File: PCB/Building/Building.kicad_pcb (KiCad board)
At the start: 2 copper layers, 95 x 60.5 mm, 37 parts, among them J1 Conn_01x05, U1 HT16K33-28SOP

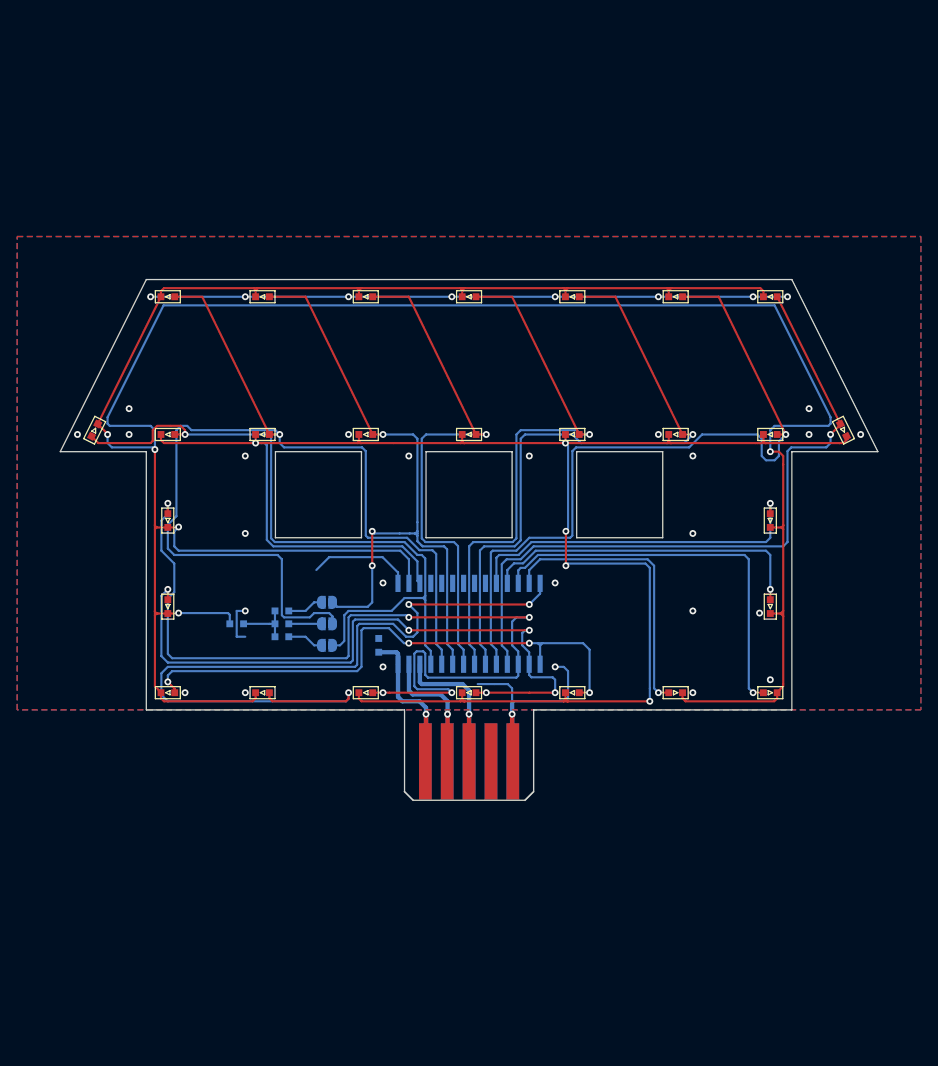
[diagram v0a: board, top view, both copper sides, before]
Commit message: (Building) 回路図内のラベルを3セット独立に修正 #75
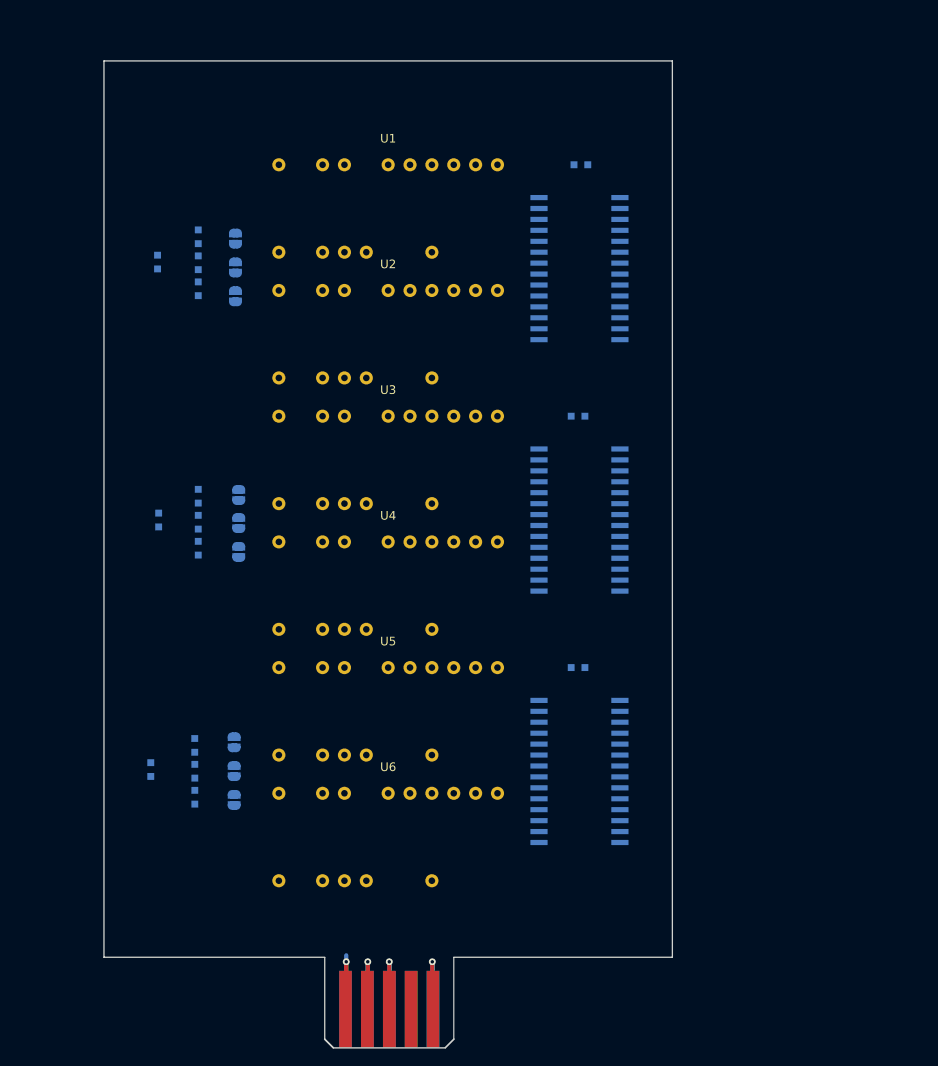
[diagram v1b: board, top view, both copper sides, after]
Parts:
- removed D10, D11, D12, D13, D14, D15, D16, D17, D18, D19, D20, D21, D22, D23, D24, D25, D26, D27, D4, D5, D6, D7, D8, D9: LED, extsui:LED_1608_HandSolderingCustom
- removed D28: D, extsui:LED_1608_HandSolderingCustom
- added C2: 0.1u, extsui:C_1608_HandSolderingCustom, B.Cu at (160.2, 65.9)
- added C3: 0.1u, extsui:C_1608_HandSolderingCustom, B.Cu at (160.2, 95.1)
- added IC1: HT16K33-28SOP, Package_SO:SOIC-28W_7.5x18.7mm_P1.27mm, B.Cu at (160.3, 48.7)
- added IC2: HT16K33-28SOP, Package_SO:SOIC-28W_7.5x18.7mm_P1.27mm, B.Cu at (160.3, 77.9)
- added IC3: HT16K33-28SOP, Package_SO:SOIC-28W_7.5x18.7mm_P1.27mm, B.Cu at (160.3, 107.2)
- added JP4: A0, Jumper:SolderJumper-2_P1.3mm_Open_RoundedPad1.0x1.5mm, B.Cu at (120.2, 110.5)
- added JP5: A1, Jumper:SolderJumper-2_P1.3mm_Open_RoundedPad1.0x1.5mm, B.Cu at (120.2, 107.1)
- added JP6: A2, Jumper:SolderJumper-2_P1.3mm_Open_RoundedPad1.0x1.5mm, B.Cu at (120.2, 103.8)
- added JP7: A0, Jumper:SolderJumper-2_P1.3mm_Open_RoundedPad1.0x1.5mm, B.Cu at (120.7, 75.0)
- added JP8: A1, Jumper:SolderJumper-2_P1.3mm_Open_RoundedPad1.0x1.5mm, B.Cu at (120.7, 78.3)
- added JP9: A2, Jumper:SolderJumper-2_P1.3mm_Open_RoundedPad1.0x1.5mm, B.Cu at (120.7, 81.6)
- added R4: 39k, extsui:R_1608_HandSolderingCustom, B.Cu at (116.0, 75.2)
- added R5: 39k, extsui:R_1608_HandSolderingCustom, B.Cu at (116.0, 78.2)
- added R6: 39k, extsui:R_1608_HandSolderingCustom, B.Cu at (116.0, 81.2)
- added R7: 39k, extsui:R_1608_HandSolderingCustom, B.Cu at (115.6, 107.1)
- added R8: 39k, extsui:R_1608_HandSolderingCustom, B.Cu at (115.6, 104.1)
- added R9: 39k, extsui:R_1608_HandSolderingCustom, B.Cu at (115.6, 110.1)
- added U2: OSL60362_IX, extsui:OSL60362_XX, F.Cu at (138.1, 56.4)
- added U3: OSL60362_IX, extsui:OSL60362_XX, F.Cu at (138.1, 71.0)
- added U4: OSL60362_IX, extsui:OSL60362_XX, F.Cu at (138.1, 85.6)
- added U5: OSL60362_IX, extsui:OSL60362_XX, F.Cu at (138.1, 100.2)
- added U6: OSL60362_IX, extsui:OSL60362_XX, F.Cu at (138.1, 114.8)
- D1, D2, D3: value LED -> D; moved to B.Cu
- JP1: value A2 -> A0
- JP3: value A0 -> A2
- U1: value HT16K33-28SOP -> OSL60362_IX; footprint Package_SO:SOIC-28W_7.5x18.7mm_P1.27mm -> extsui:OSL60362_XX; moved to F.Cu
- moved C1 60.6 mm to (160.5, 36.7), turned to 0 degrees
- moved D3 56.4 mm to (110.5, 106.9), turned to 90 degrees
- moved U1 49.2 mm to (138.1, 41.7), turned to 0 degrees
- moved JP1 48.4 mm to (120.4, 45.2), turned to 90 degrees
- moved R1 47.5 mm to (116.0, 45.0), turned to 90 degrees
- moved R2 43.1 mm to (116.0, 48.1), turned to 90 degrees
- moved JP2 42.8 mm to (120.4, 48.6), turned to 90 degrees
- moved R3 38.7 mm to (116.0, 51.1), turned to 90 degrees
- moved JP3 37.1 mm to (120.4, 51.9), turned to 90 degrees
- moved J1 30.2 mm to (138.2, 134.8)
- moved D2 26.0 mm to (111.4, 77.9), turned to 90 degrees
- moved D1 20.9 mm to (111.3, 48.0), turned to 90 degrees
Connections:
- D1 pad 2: Net-(D1-Pad2) -> /A_1
- D2 pad 1: Net-(D1-Pad1) -> Net-(D2-Pad1)
- D2 pad 2: Net-(D18-Pad2) -> /A_2
- D3 pad 1: Net-(D1-Pad1) -> Net-(D3-Pad1)
- D3 pad 2: Net-(D19-Pad2) -> /A_3
- JP1 pad 2: Net-(D1-Pad2) -> /CA3
- JP2 pad 2: Net-(D18-Pad2) -> /CA2
- JP3 pad 2: Net-(D19-Pad2) -> /CA1
- R1 pad 2: Net-(D28-Pad1) -> Net-(D1-Pad1)
- R2 pad 2: Net-(D28-Pad1) -> Net-(D1-Pad1)
- R3 pad 2: Net-(D28-Pad1) -> Net-(D1-Pad1)
- U1 pad 1: GND -> /E_1
- U1 pad 12: Net-(D14-Pad2) -> /CA6
- U1 pad 13: Net-(D13-Pad2) -> /CA5
- U1 pad 14: Net-(D12-Pad2) -> /F_1
- U1 pad 15: Net-(D11-Pad2) -> /A_1
- U1 pad 16: Net-(D10-Pad2) -> /CA4
- U1 pad 17: Net-(D25-Pad2) -> /G_1
- U1 pad 19: Net-(D23-Pad2) -> /C_1
- U1 pad 20: Net-(D22-Pad2) -> /B_1
- U1 pad 22: Net-(D20-Pad2) -> /CA1
- U1 pad 3: Net-(D17-Pad1) -> /CA2
- U1 pad 4: Net-(U1-Pad4) -> /CA3
- U1 pad 5: Net-(U1-Pad5) -> /D_1
- U1 pad 8: Net-(U1-Pad8) -> /DP_1
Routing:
- net Net-(D1-Pad1): track 357.3 -> 0.00 mm, vias 5 -> 0
- net Net-(D17-Pad1): track 201.4 -> 0.00 mm, vias 5 -> 0
- net Net-(D18-Pad2): track 119.8 -> 0.00 mm, vias 1 -> 0
- net Net-(D25-Pad2): track 108.4 -> 0.00 mm, vias 5 -> 0
- net GND: track 120.7 -> 12.3 mm, vias 34 -> 1
- net Net-(D12-Pad2): track 92.7 -> 0.00 mm, vias 3 -> 0
- net Net-(D23-Pad2): track 86.6 -> 0.00 mm, vias 1 -> 0
- net Net-(D1-Pad2): track 83.3 -> 0.00 mm, vias 1 -> 0
- net Net-(D24-Pad2): track 81.3 -> 0.00 mm, vias 1 -> 0
- net Net-(D10-Pad2): track 77.7 -> 0.00 mm, vias 5 -> 0
- net Net-(D19-Pad2): track 76.1 -> 0.00 mm, vias 3 -> 0
- net Net-(D22-Pad2): track 74.7 -> 0.00 mm, vias 1 -> 0
- net Net-(D11-Pad2): track 67.3 -> 0.00 mm, vias 4 -> 0
- net Net-(D21-Pad2): track 64.0 -> 0.00 mm, vias 1 -> 0
- net Net-(D20-Pad2): track 61.1 -> 0.00 mm, vias 1 -> 0
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- removed copper zone on B.Cu, net GND
- removed copper zone on F.Cu, net GND
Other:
- board size 95 x 60.5 mm -> 66 x 114.7 mm
- net class Default added: clearance 0.2, trace_width 0.25, via_dia 0.8, via_drill 0.4
- board text removed: "1"
- board text removed: "5"
- board text removed: "@ext_sui 2020.03"
- board text removed: "Building Growing v1.0"

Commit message: (Building) 基板上にパーツを仮配置 #75
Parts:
- moved JP7 58.3 mm to (162.2, 116.0), turned to 0 degrees
- moved JP8 57.8 mm to (162.2, 118.6), turned to 0 degrees
- moved JP9 57.3 mm to (162.2, 121.1), turned to 0 degrees
- moved D3 48.4 mm to (158.4, 113.5), turned to 180 degrees
- moved JP4 47.6 mm to (161.6, 86.8), turned to 0 degrees
- moved D1 47.0 mm to (157.8, 55.1), turned to 0 degrees
- moved D2 46.8 mm to (157.8, 84.3), turned to 180 degrees
- moved R8 45.2 mm to (158.4, 118.6), turned to 180 degrees
- moved JP5 45.0 mm to (161.6, 89.4), turned to 0 degrees
- moved R9 44.2 mm to (158.4, 121.1), turned to 180 degrees
- moved R7 43.7 mm to (158.4, 116.0), turned to 180 degrees
- moved R1 43.6 mm to (157.7, 57.6), turned to 180 degrees
- moved R2 43.4 mm to (157.7, 60.1), turned to 180 degrees
- moved R4 43.3 mm to (157.8, 86.8), turned to 180 degrees
- moved R3 43.3 mm to (157.7, 62.7), turned to 180 degrees
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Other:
- board size 66 x 114.7 mm -> 61 x 112.1 mm

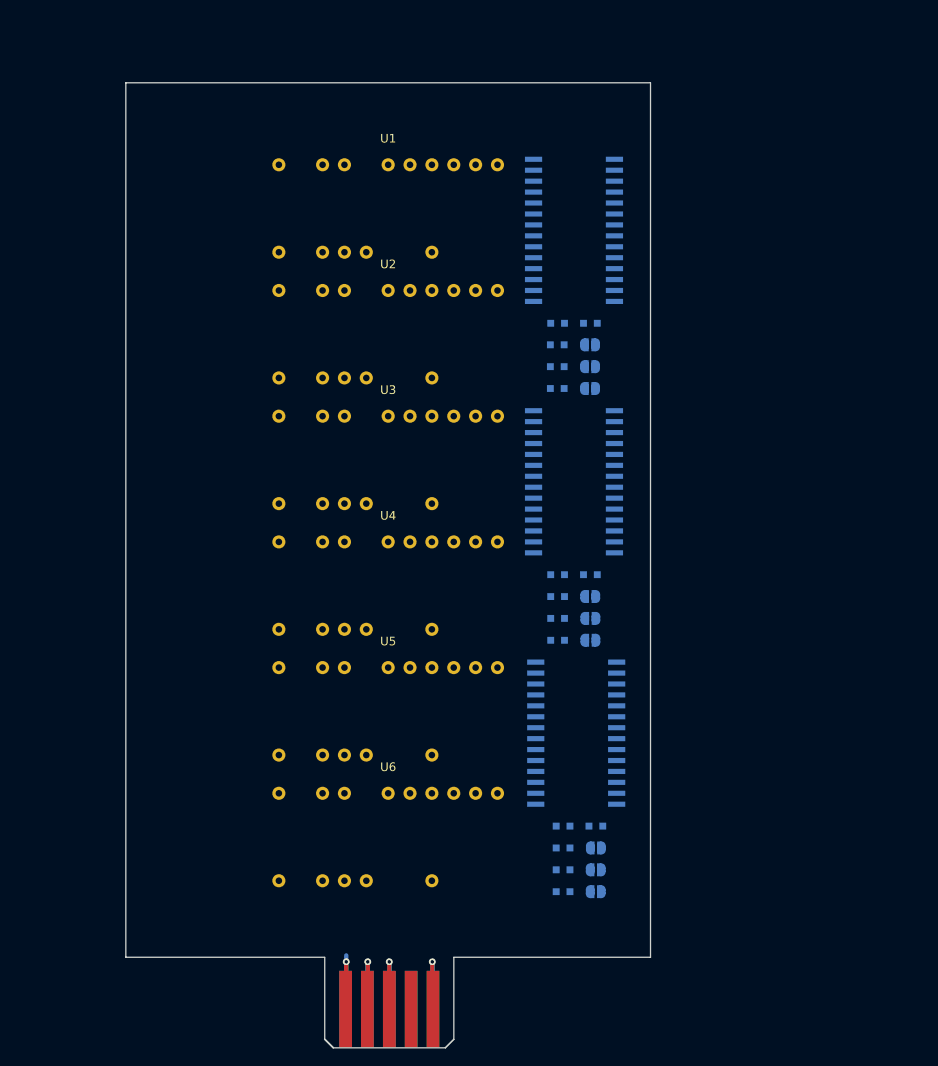
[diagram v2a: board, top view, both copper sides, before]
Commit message: (Building) OSL60362_XX のシルクが別レイヤになっていたのを修正 #75
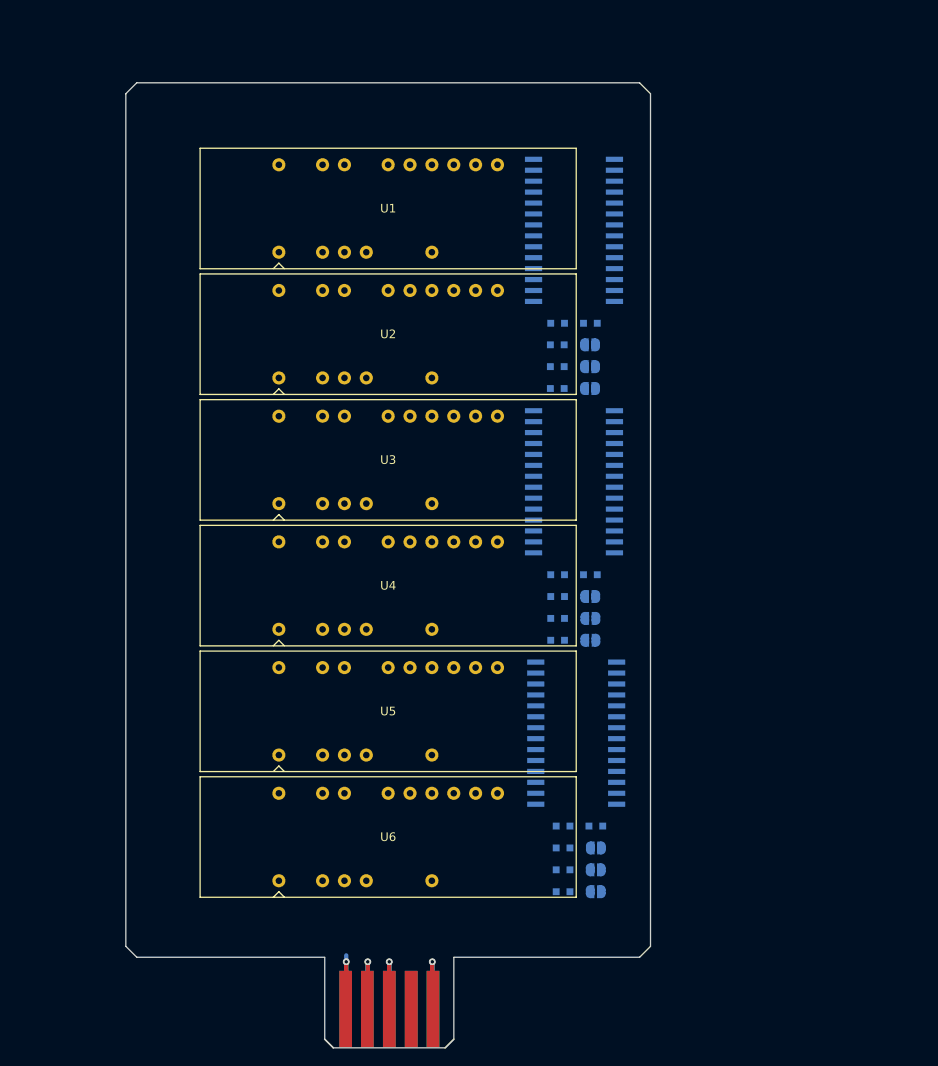
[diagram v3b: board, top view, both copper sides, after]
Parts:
- turned D2 to 0 degrees
- turned D3 to 0 degrees
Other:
- outline, holes or cut-outs redrawn

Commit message: (Building) 1ユニット目の仮配線完了 #75
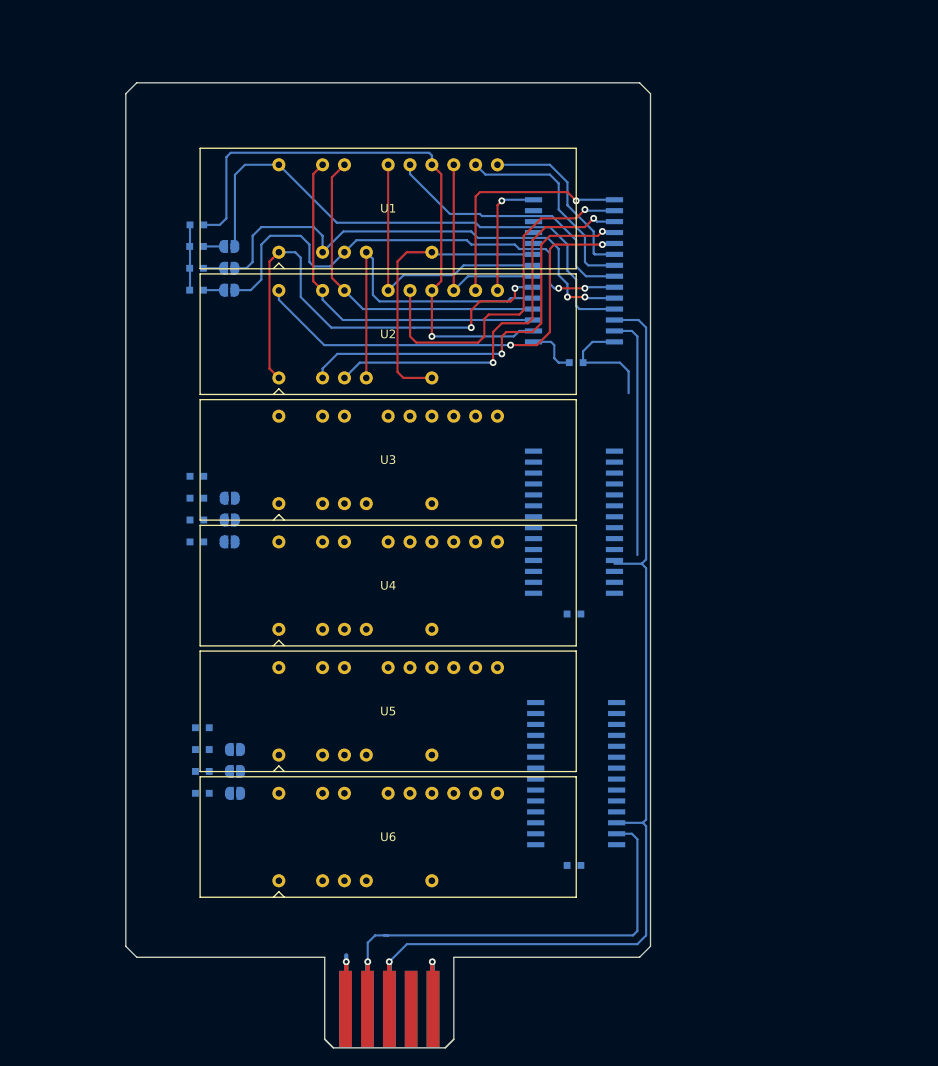
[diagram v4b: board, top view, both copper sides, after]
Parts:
- moved JP3 45.0 mm to (119.6, 46.2)
- moved JP9 45.0 mm to (120.3, 104.6)
- moved R3 45.0 mm to (115.8, 46.2)
- moved JP6 45.0 mm to (119.7, 75.4)
- moved R6 45.0 mm to (115.9, 75.4)
- moved R9 45.0 mm to (116.5, 104.6)
- moved D2 43.4 mm to (115.9, 72.9)
- moved JP5 43.4 mm to (119.7, 77.9)
- moved R5 43.4 mm to (115.9, 77.9)
- moved D1 43.4 mm to (115.9, 43.6)
- moved JP2 43.4 mm to (119.6, 48.7)
- moved JP8 43.4 mm to (120.3, 107.2)
- moved R2 43.4 mm to (115.8, 48.7)
- moved D3 43.4 mm to (116.5, 102.1)
- moved R8 43.4 mm to (116.5, 107.2)
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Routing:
- net SCL: track 12.5 -> 125.2 mm
- net SDA: track 12.5 -> 88.8 mm
- net /A_1: track 0.00 -> 68.3 mm, vias 0 -> 1
- net /CA1: track 0.00 -> 63.4 mm
- net /CA3: track 0.00 -> 57.5 mm, vias 0 -> 2
- net /CA2: track 0.00 -> 57.1 mm, vias 0 -> 2
- net /E_1: track 0.00 -> 55.8 mm, vias 0 -> 2
- net /CA7: track 0.00 -> 52.8 mm, vias 0 -> 2
- net /CA8: track 0.00 -> 48.2 mm, vias 0 -> 2
- net /CA9: track 0.00 -> 46.6 mm, vias 0 -> 2
- net /CA10: track 0.00 -> 42.1 mm, vias 0 -> 1
- net /B_1: track 0.00 -> 42.1 mm
- net /D_1: track 0.00 -> 39.0 mm
- net /C_1: track 0.00 -> 38.7 mm
- net /DP_1: track 0.00 -> 33.5 mm
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
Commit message: (Building) 配線最適化1 #75
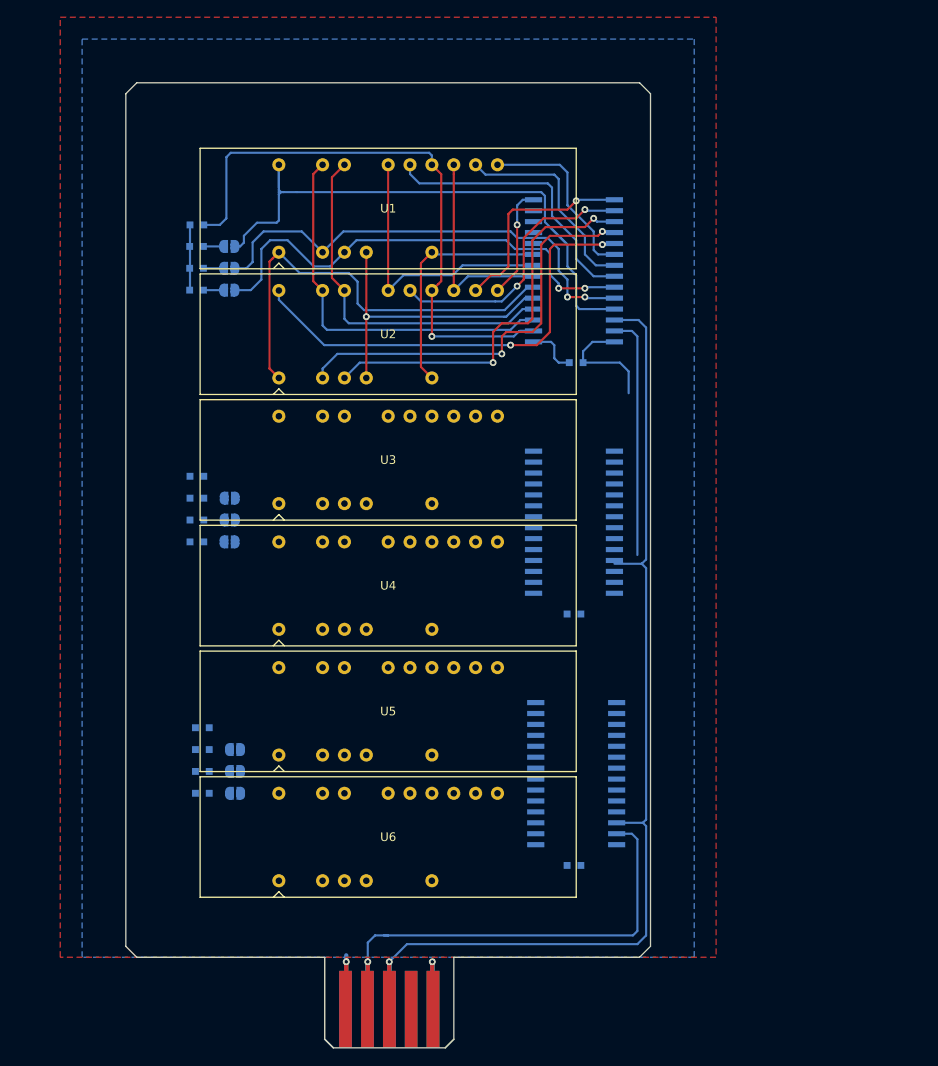
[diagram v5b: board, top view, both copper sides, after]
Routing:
- net /CA10: track 42.1 -> 31.6 mm, vias 1 -> 2
- net /CA1: track 63.4 -> 69.5 mm
- net /DP_1: track 33.5 -> 27.6 mm
- net /E_1: track 55.8 -> 51.2 mm, vias 2 -> 0
- net /D_1: track 39.0 -> 34.9 mm, vias 0 -> 1
- net /CA11: track 27.7 -> 24.1 mm
- net /C_1: track 38.7 -> 42.0 mm
- net /B_1: track 42.1 -> 44.8 mm
- net /CA3: track 57.5 -> 55.3 mm
- net /CA2: track 57.1 -> 55.1 mm
- net /A_1: track 68.3 -> 69.8 mm
- net /CA4: track 31.5 -> 32.9 mm
- net /CA12: track 14.4 -> 13.0 mm
- added copper zone on B.Cu, net GND
- added copper zone on F.Cu, net GND
